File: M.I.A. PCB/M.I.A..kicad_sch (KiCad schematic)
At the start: 44 parts, among them J1 USB_C_Receptacle_USB2.0_16P, SW1 SW_Push, SW2 SW_Push, U1 W25Q128JVS, U2 RP2350B-QFN80, Y1 ABM8-272-T3

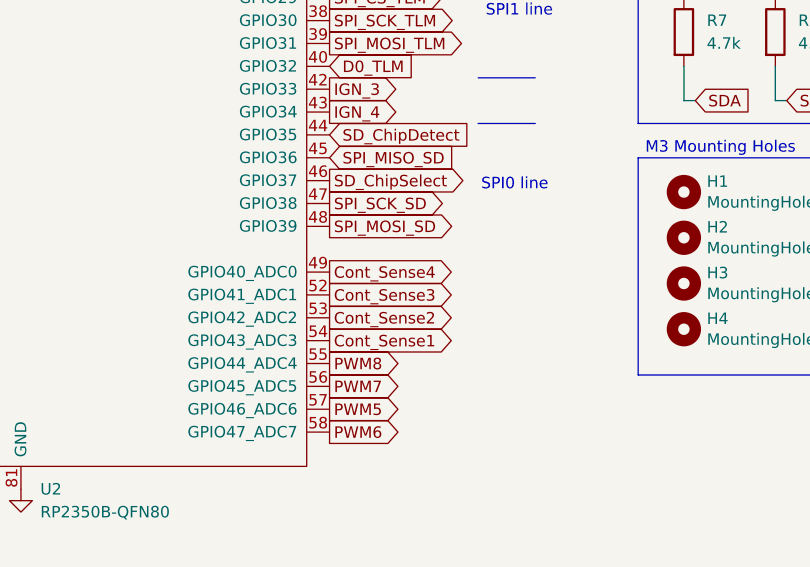
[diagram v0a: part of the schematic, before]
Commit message: routed ign3/4, fixed some drc
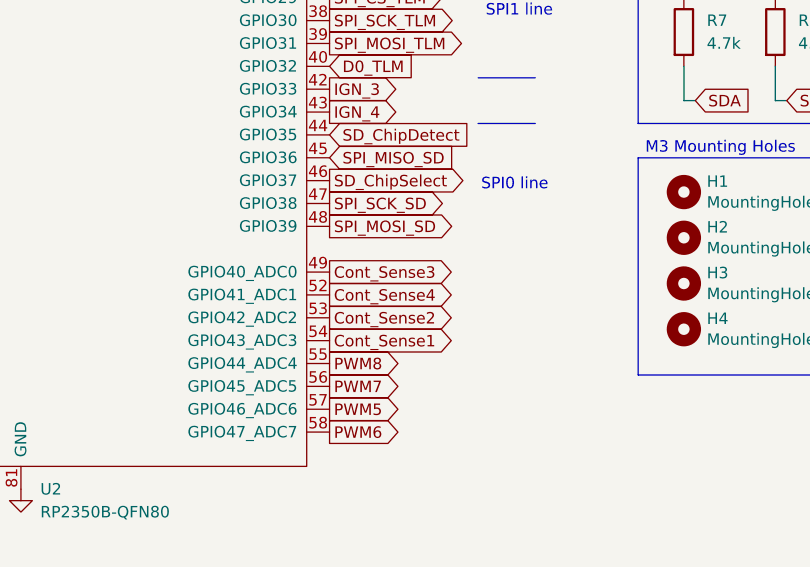
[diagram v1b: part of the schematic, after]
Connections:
- net Cont_Sense3: now also U2.49 (GPIO40_ADC0); no longer U2.52 (GPIO41_ADC1)
- net Cont_Sense4: now also U2.52 (GPIO41_ADC1); no longer U2.49 (GPIO40_ADC0)
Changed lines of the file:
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@@
 	(global_label "Cont_Sense3"
 		(shape output)
-		(at 166.37 156.21 0)
-		(fields_autoplaced yes)
-		(effects
-			(font
-				(size 1.27 1.27)
-			)
-			(justify left)
-		)
-		(property "Intersheetrefs" "${INTERSHEET_REFS}"
-			(at 181.3898 156.21 0)
+		(at 166.37 153.67 0)
+		(fields_autoplaced yes)
+		(effects
+			(font
+				(size 1.27 1.27)
+			)
+			(justify left)
+		)
+		(property "Intersheetrefs" "${INTERSHEET_REFS}"
+			(at 181.3898 153.67 0)
 			(effects
 				(font
@@
 	(global_label "Cont_Sense4"
 		(shape output)
-		(at 166.37 153.67 0)
-		(fields_autoplaced yes)
-		(effects
-			(font
-				(size 1.27 1.27)
-			)
-			(justify left)
-		)
-		(property "Intersheetrefs" "${INTERSHEET_REFS}"
-			(at 181.3898 153.67 0)
-			(effects
-				(font
+		(at 166.37 156.21 0)
+		(fields_autoplaced yes)
+		(effects
+			(font
+				(size 1.27 1.27)
+			)
+			(justify left)
+		)
+		(property "Intersheetrefs" "${INTERSHEET_REFS}"
+			(at 181.3898 156.21 0)
+			(effects
+				(font

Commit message: Final Fixes, impedances, silkscreen etc
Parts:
- R2, R3: value 22 -> 27
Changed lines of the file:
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@@
 			)
 		)
-		(property "Value" "22"
+		(property "Value" "27"
 			(at 184.15 37.084 90)
 			(effects
@@
 			)
 		)
-		(property "Value" "22"
+		(property "Value" "27"
 			(at 184.15 46.736 90)
 			(effects

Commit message: More Small Updates/Improvements
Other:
- note added: "ICM42688-PC IMU MMC5983MA Magnetometer KX134 High-G Accelerometer MS5611 Barometer TMP117 Temperature Sensor MAX-M10S GPS"
- note added: "INA219 Power Sensor, AP62150 Switching Regulators, AP212K Linear Regulator TPS2121 Power OR"
- note added: "MicroSD Card, Servo Connectors, Telemetry Radio, Ignition lines, RGB LEDs, Other Connectors"
- note removed: "ICM42688-PC IMU MMC5983MA Magnetometer KX134 High-G Accelerometer MS5611 Barometer"
- note removed: "MicroSD Card, Servo Connectors, Telemetry Radio"
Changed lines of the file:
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@@
 		)
 	)
-	(text "MicroSD Card,\nServo Connectors,\nTelemetry Radio\n\n"
+	(text "MicroSD Card,\nServo Connectors,\nTelemetry Radio,\nIgnition lines,\nRGB LEDs,\nOther Connectors\n\n"
 		(exclude_from_sim no)
-		(at 233.172 132.842 0)
+		(at 232.664 126.746 0)
 		(effects
 			(font
 				(size 1.905 1.905)
 			)
-			(justify left)
+			(justify left top)
 		)
 	)
@@
 		)
 	)
-	(text "ICM42688-PC IMU\nMMC5983MA Magnetometer\nKX134 High-G Accelerometer\nMS5611 Barometer\n"
+	(text "ICM42688-PC IMU\nMMC5983MA Magnetometer\nKX134 High-G Accelerometer\nMS5611 Barometer\nTMP117 Temperature Sensor\nMAX-M10S GPS"
 		(exclude_from_sim no)
-		(at 233.172 91.186 0)
+		(at 232.918 93.98 0)
 		(effects
 			(font
@@
 		)
 	)
+	(text "INA219 Power Sensor,\nAP62150 Switching Regulators,\nAP212K Linear Regulator\nTPS2121 Power OR"
+		(exclude_from_sim no)
+		(at 233.172 49.022 0)
+		(effects
+			(font
+				(size 1.905 1.905)
+			)
+			(justify left)
+		)
+	)
